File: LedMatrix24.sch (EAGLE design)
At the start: 87 parts, among them IC1 74HC595N, IC11 74HC595N, IC2 74HC595N, IC3 74HC595N, IC4 UDN2981A, IC5 UDN2981A, IC6 74HC595N, IC8 UDN2981A, IC9 74HC595N

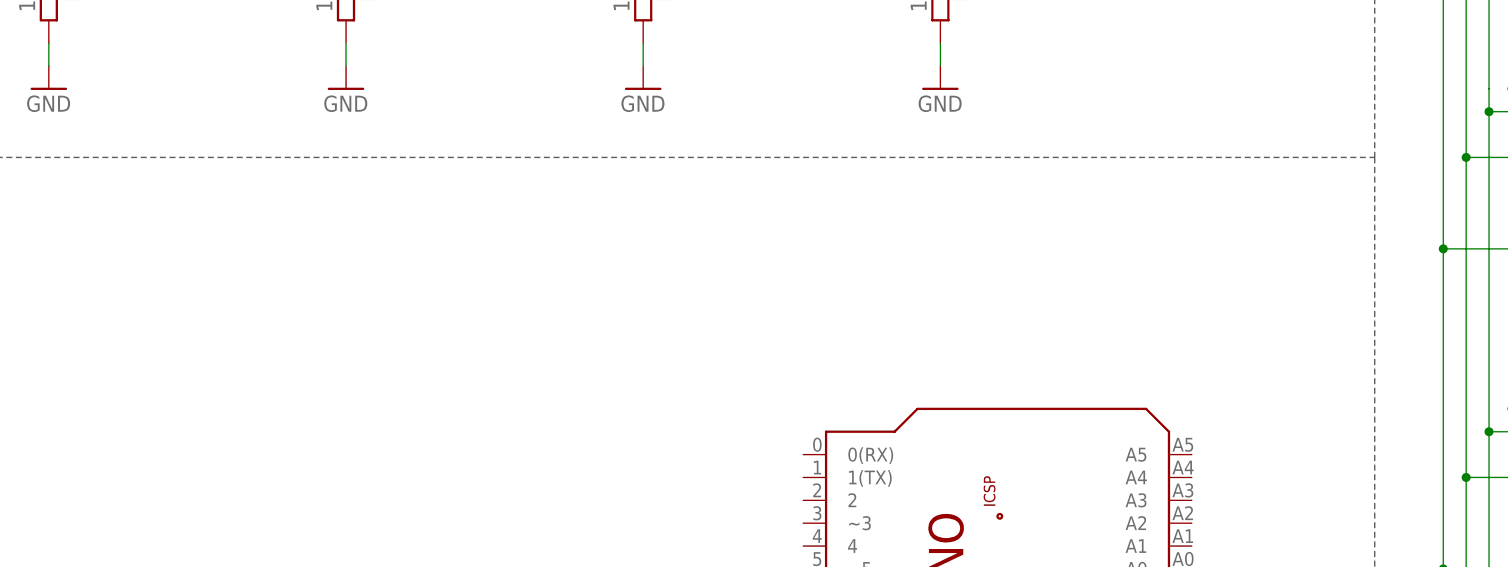
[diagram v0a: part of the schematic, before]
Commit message: LED Matrizen an Raster 2.5mm angepasst und Buzzer eingefügt
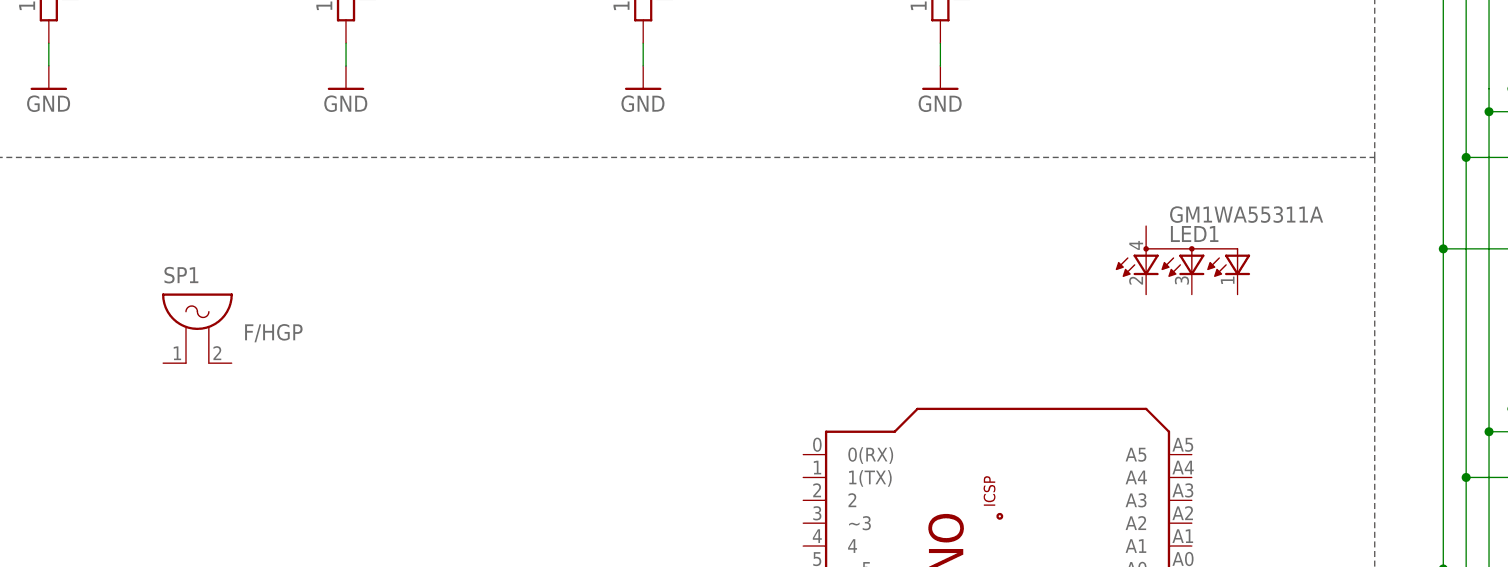
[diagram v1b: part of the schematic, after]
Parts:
- added LED1: GM1WA55311A, led:GM1WA55311A
- added SP1: F/HGP, buzzer:F/HGP
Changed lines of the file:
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@@
 <?xml version="1.0" encoding="utf-8"?>
 <!DOCTYPE eagle SYSTEM "eagle.dtd">
-<eagle version="7.5.0">
+<eagle version="7.7.0">
 <drawing>
 <settings>
@@
 <part name="P+20" library="supply1" deviceset="+5V" device=""/>
 <part name="PCB1" library="E14_Arduino_revC" deviceset="ARDUINO_UNO" device=""/>
+<part name="SP1" library="buzzer" deviceset="F/HGP" device=""/>
+<part name="LED1" library="led" deviceset="GM1WA55311A" device=""/>
 </parts>
 <sheets>
@@
 <instance part="P+20" gate="1" x="22.86" y="43.18"/>
 <instance part="PCB1" gate="G$1" x="134.62" y="58.42" rot="R90"/>
+<instance part="SP1" gate="G$1" x="45.72" y="96.52"/>
+<instance part="LED1" gate="G$1" x="157.48" y="106.68"/>
 </instances>
 <busses>
